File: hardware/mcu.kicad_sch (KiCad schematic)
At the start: 0 parts

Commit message: ✨ Further power supply schematic
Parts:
- added U1: ~, PCM_Espressif:ESP32-P4, symbol PCM_Espressif:ESP32-P4

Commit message: ✨ Further schematic updates
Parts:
- added C29: 100nF/10V, symbol Device:C
- added R13: 10k, symbol Device:R
- added U7: W25Q128JVP, Package_SON:WSON-8-1EP_6x5mm_P1.27mm_EP3.4x4.3mm, symbol Memory_Flash:W25Q128JVP
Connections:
- net +3.3VA: now reaches U1.101 (VDD_ANA)
- net +3.3V: now reaches U1.102 (VDD_BAT)
- net +3.3V: now also U1.21 (VDD_IO_0), U1.30 (VDD_FLASH_IO), U1.51 (VDD_USBPHY), U1.62 (VDD_IO_4), U1.75 (VDD_LDO), U1.85 (VDD_IO_5), U1.9 (VDD_LP), U1.96 (VDD_IO_6), C29.1, R13.1, U7.8 (VCC)
- net GND: now reaches U1.105 (GND)
- net GND: now also C29.2, U7.4 (GND), U7.9 (EP)
- net +1V2: now reaches U1.26 (VDD_HP_0)
- net +1V2: now also U1.76 (VDD_HP_2), U1.91 (VDD_HP_3)
- net FLASH_CS: now reaches U1.27 (FLASH_CS)
- net FLASH_CS: now also R13.2, U7.1 (~{CS})
- net FLASH_Q: now reaches U1.28 (FLASH_Q)
- net FLASH_Q: now also U7.2 (DO/IO_{1})
- net FLASH_WP: now reaches U1.29 (FLASH_WP)
- net FLASH_WP: now also U7.3 (~{WP}/IO_{2})
- net FLASH_HOLD: now reaches U1.31 (FLASH_HOLD)
- net FLASH_HOLD: now also U7.7 (~{HOLD}/~{RESET}/IO_{3})
- net FLASH_CK: now reaches U1.32 (FLASH_CK)
- net FLASH_CK: now also U7.6 (CLK)
- net FLASH_D: now reaches U1.33 (FLASH_D)
- net FLASH_D: now also U7.5 (DI/IO_{0})
- net +2V5: now reaches U1.41 (VDD_MIPI_DPHY)
- net FB_DCDC: now reaches U1.78 (FB_DCDC)
- net EN_DCDC: now reaches U1.79 (EN_DCDC)

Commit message: ✨ MCU updates
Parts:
- added C39, C40: 12pF, symbol Device:C
- added C41, C42, C43, C44: 1uF, symbol Device:C
- added C45, C46, C47, C48, C49, C50, C51, C52, C53, C54, C55, C56, C57, C58, C59, C60: 100nF, symbol Device:C
- added R21, R22: 0, symbol Device:R
- added R23: 4.02k, symbol Device:R
- added X1: ECS-400-10-37B2-CKY-TR, Crystal:Crystal_SMD_2016-4Pin_2.0x1.6mm, symbol PCM_Crystal_AKL:Crystal_Generic_GND24
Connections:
- net +1V2: now also C46.1, C49.1, C50.1
- net +2V5: now also C52.1
- net +3.3V: now also U1.77 (VDD_DCDCC), C45.1, C51.1, C53.1, C54.1, C55.1, C56.1, C57.1, C59.1, C60.1
- net +3.3VA: now also C58.1
- net GND: now also C39.2, C40.2, C41.2, C42.2, C43.2, C44.2, C45.2, C46.2, C47.2, C48.2, C49.2, C50.2, C51.2, C52.2, C53.2, C54.2, C55.2, C56.2, C57.2, C58.2, C59.2, C60.2, R23.2, X1.2, X1.4
- net XTAL_P: now reaches U1.100 (XTAL_P)
- net XTAL_P: now also R21.1
- net at U1.34 (DSI_REXT): now also R23.1
- net VDDO_PSRAM: now reaches U1.59 (VDD_PSRAM_0)
- net VDDO_PSRAM: now also U1.67 (VDD_PSRAM_1), U1.72 (VDDO_PSRAM), C42.1, C47.1, C48.1
- net VDDO_FLASH: now reaches U1.71 (VDDO_FLASH)
- net VDDO_FLASH: now also C41.1
- net VDDO_3: now reaches U1.73 (VDDO_3)
- net VDDO_3: now also C43.1
- net VDDO_4: now reaches U1.74 (VDDO_4)
- net VDDO_4: now also C44.1
- net XTAL_N: now reaches U1.99 (XTAL_N)
- net XTAL_N: now also R22.2
- new net: C39.1, R21.2, X1.1
- new net: C40.1, R22.1, X1.3

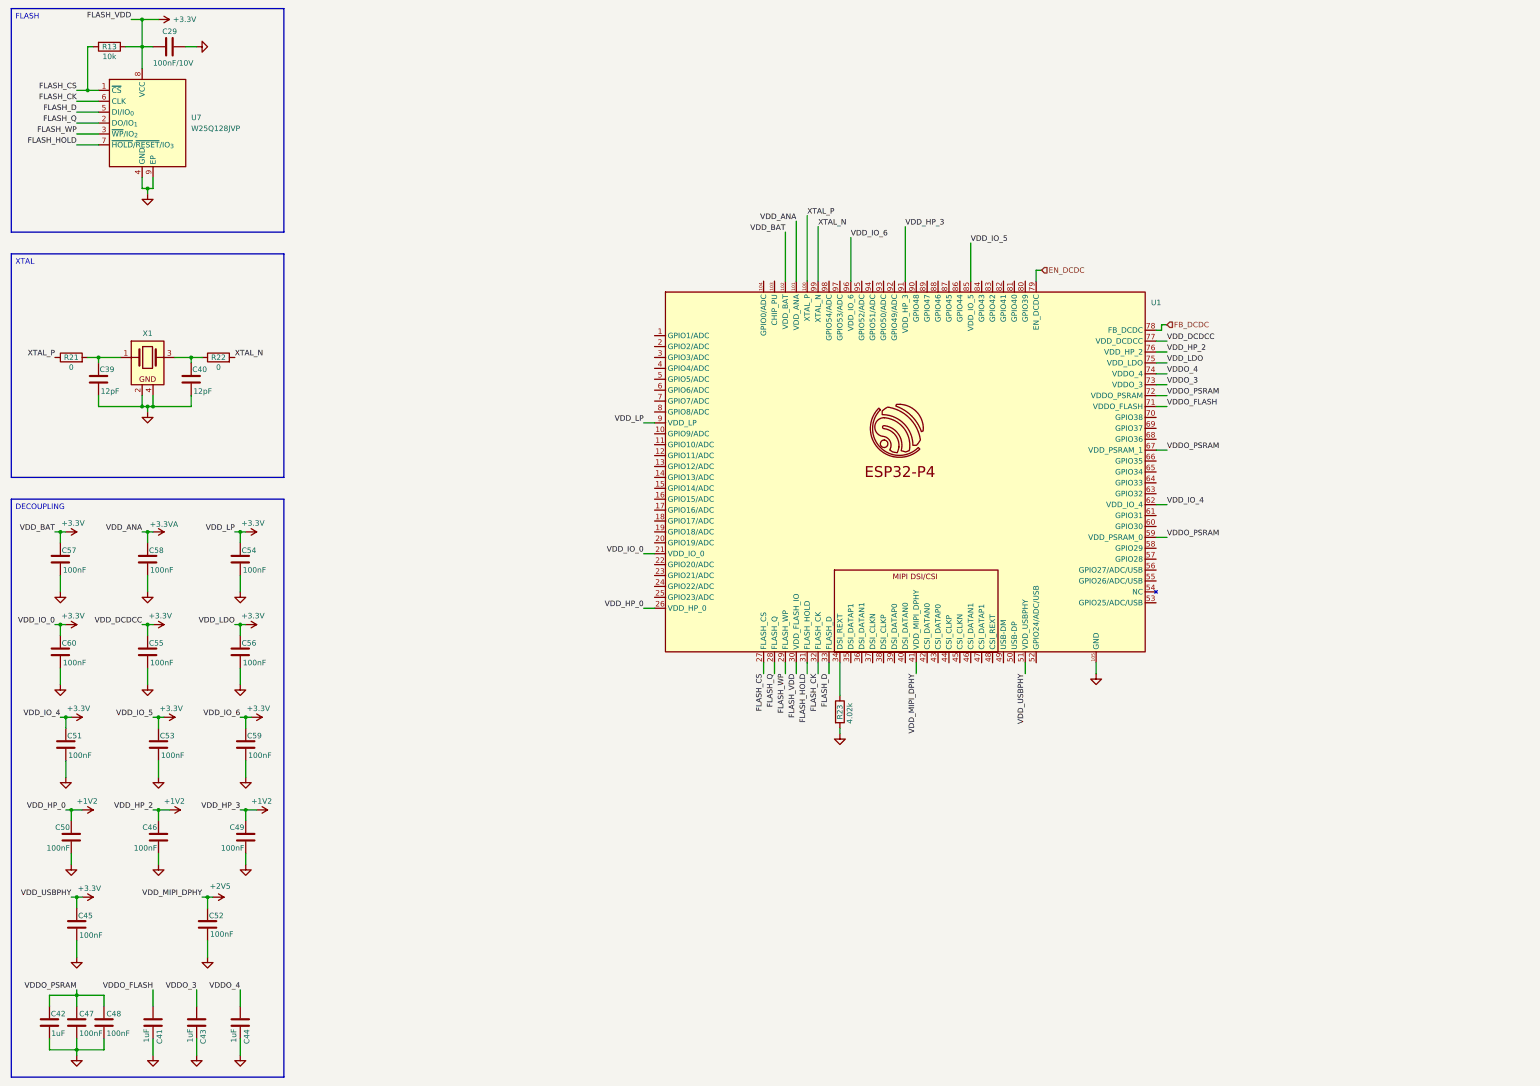
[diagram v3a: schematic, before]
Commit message: ✨ Done wireless schematic
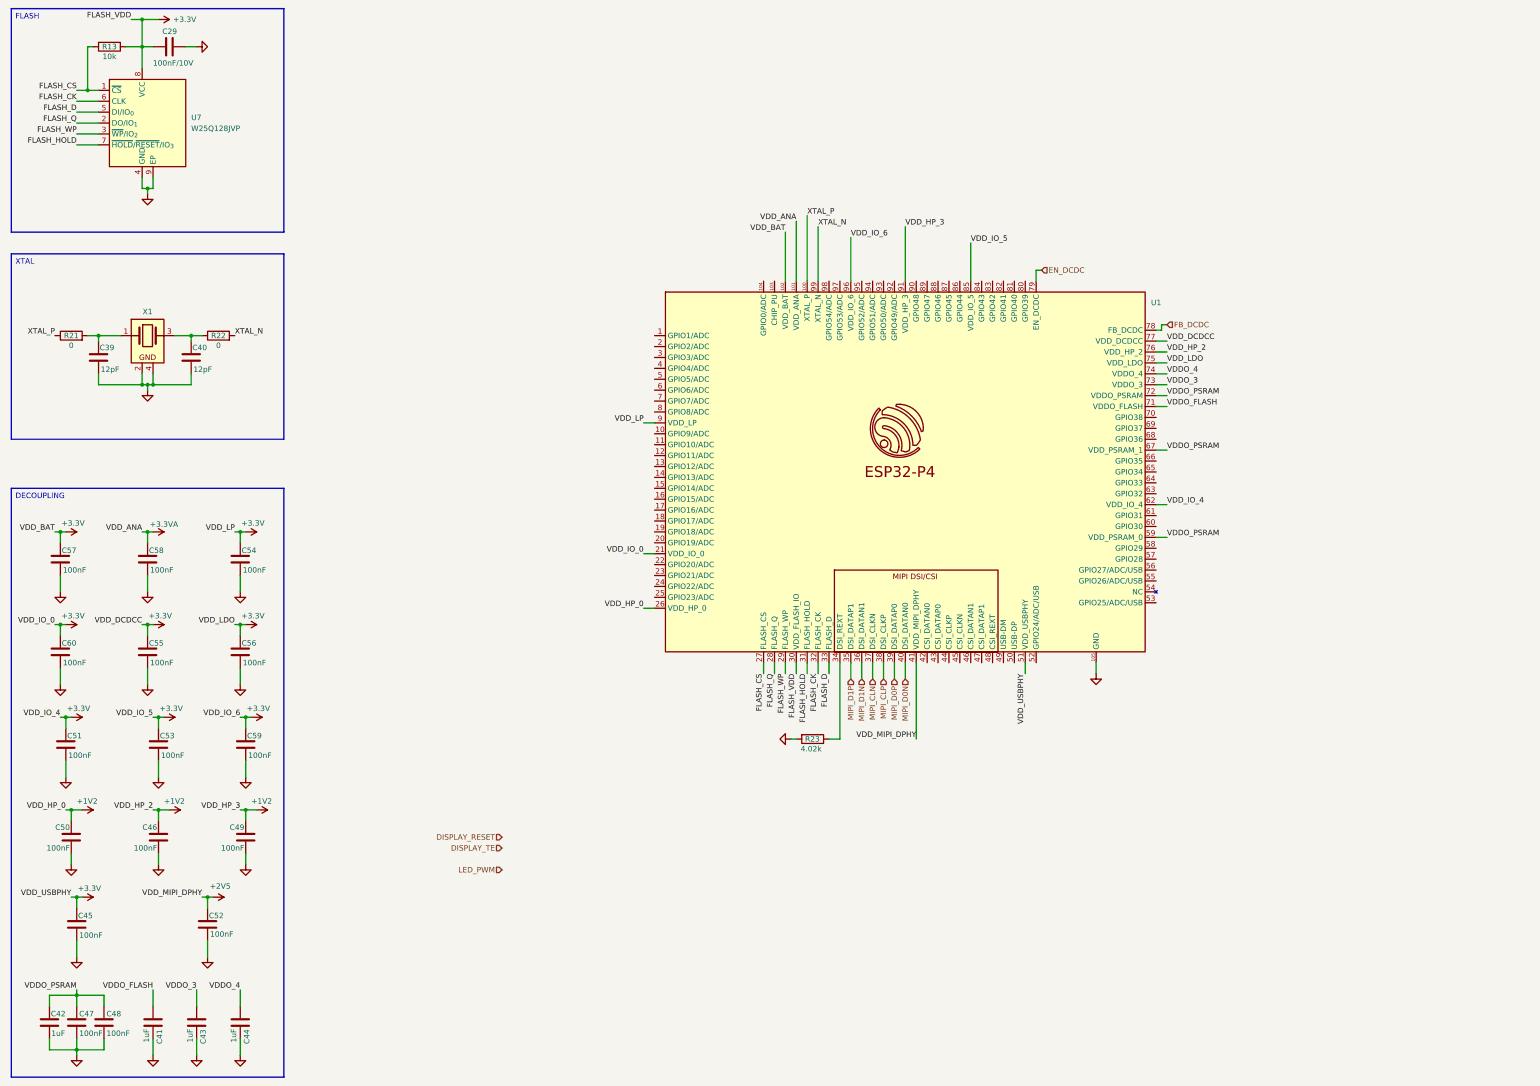
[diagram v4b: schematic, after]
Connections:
- net MIPI_D1P: now reaches U1.35 (DSI_DATAP1)
- net MIPI_D1N: now reaches U1.36 (DSI_DATAN1)
- net MIPI_CLN: now reaches U1.37 (DSI_CLKN)
- net MIPI_CLP: now reaches U1.38 (DSI_CLKP)
- net MIPI_D0P: now reaches U1.39 (DSI_DATAP0)
- net MIPI_D0N: now reaches U1.40 (DSI_DATAN0)
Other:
- moved on the sheet: C39, C40, R21, R22, R23, X1

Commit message: 📂 PCB updates
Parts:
- added C18: 1uF, Capacitor_SMD:C_0402_1005Metric, symbol Device:C
- added J4: Conn_DEBUG_P4, Connector_JST:JST_SHL_SM06B-SHLS-TF_1x06-1MP_P1.00mm_Horizontal, symbol Connector_Generic:Conn_01x06
- added R36, R37, R38, R39, R40, R41: 0, PCM_Resistor_SMD_AKL:R_0402_1005Metric, symbol Device:R
- added R42, R43: 4.7k, PCM_Resistor_SMD_AKL:R_0402_1005Metric, symbol Device:R
- added R44, R45: 10k, PCM_Resistor_SMD_AKL:R_0402_1005Metric, symbol Device:R
- C29: value 100nF/10V -> 100nF; footprint (none) -> Capacitor_SMD:C_0402_1005Metric
- C39, C40, C41, C42, C43, C44, C45, C46, C47, C48, C49, C50, C51, C52, C53, C54, C55, C56, C57, C58, C59, C60: footprint (none) -> Capacitor_SMD:C_0402_1005Metric
- R13, R21, R22, R23: footprint (none) -> PCM_Resistor_SMD_AKL:R_0402_1005Metric
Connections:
- net +3.3V: now also R42.2, R43.2, R44.1, R45.1
- net DISPLAY_RESET: now also U1.57 (GPIO28)
- net DISPLAY_TE: now also U1.56 (GPIO27/ADC/USB)
- net GND: now also C18.2, J4.6 (Pin_6)
- net LED_PWM: now also U1.55 (GPIO26/ADC/USB)
- net MIPI_CLN: now also R38.1; no longer U1.37 (DSI_CLKN)
- net MIPI_CLP: now also R39.1; no longer U1.38 (DSI_CLKP)
- net MIPI_D0N: now also R41.1; no longer U1.40 (DSI_DATAN0)
- net MIPI_D0P: now also R40.1; no longer U1.39 (DSI_DATAP0)
- net MIPI_D1N: now also R37.1; no longer U1.36 (DSI_DATAN1)
- net MIPI_D1P: now also R36.1; no longer U1.35 (DSI_DATAP1)
- net SW_MCU: now reaches U1.10 (GPIO9/ADC)
- net EN: now reaches U1.103 (CHIP_PU)
- net EN: now also C18.1, J4.2 (Pin_2), R44.2
- net SDIO_DATA0: now reaches U1.15 (GPIO14/ADC)
- net SDIO_DATA1: now reaches U1.16 (GPIO15/ADC)
- net SDIO_DATA2: now reaches U1.17 (GPIO16/ADC)
- net SDIO_DATA3: now reaches U1.18 (GPIO17/ADC)
- net SDIO_CLK: now reaches U1.19 (GPIO18/ADC)
- net SDIO_CMD: now reaches U1.20 (GPIO19/ADC)
- net RX_CAN: now reaches U1.23 (GPIO21/ADC)
- net TX_CAN: now reaches U1.24 (GPIO22/ADC)
- net JTAG_DN: now reaches U1.49 (USB-DM)
- net JTAG_DN: now also J4.5 (Pin_5)
- net JTAG_DP: now reaches U1.50 (USB-DP)
- net JTAG_DP: now also J4.4 (Pin_4)
- net BUTTON_U: now reaches U1.6 (GPIO6/ADC)
- net SCL_MCU: now reaches U1.60 (GPIO30)
- net SCL_MCU: now also R43.1
- net SDA_MCU: now reaches U1.61 (GPIO31)
- net SDA_MCU: now also R42.1
- net BOOT: now reaches U1.66 (GPIO35)
- net BOOT: now also J4.3 (Pin_3)
- net at U1.68 (GPIO36): now also R45.2
- net BUTTON_P: now reaches U1.7 (GPIO7/ADC)
- net BUTTON_D: now reaches U1.8 (GPIO8/ADC)
- net VBUS_MCU: now reaches U1.92 (GPIO49/ADC)
- new net +5V: J4.1 (Pin_1)
- new net MIPI_MCU_CLN: R38.2, U1.37 (DSI_CLKN)
- new net MIPI_MCU_CLP: R39.2, U1.38 (DSI_CLKP)
- new net MIPI_MCU_D0N: R41.2, U1.40 (DSI_DATAN0)
- new net MIPI_MCU_D0P: R40.2, U1.39 (DSI_DATAP0)
- new net MIPI_MCU_D1N: R37.2, U1.36 (DSI_DATAN1)
- new net MIPI_MCU_D1P: R36.2, U1.35 (DSI_DATAP1)

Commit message: 🐛 Fix errors from rev1.0
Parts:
- removed C52: 100nF, Capacitor_SMD:C_0402_1005Metric, symbol Device:C
- added C10: 100nF, Capacitor_SMD:C_0402_1005Metric, symbol Device:C
- added R46, R47: 33, PCM_Resistor_SMD_AKL:R_0603_1608Metric, symbol Device:R
- added R48: 4.02k, PCM_Resistor_SMD_AKL:R_0402_1005Metric, symbol Device:R
- added R51: 10k, PCM_Resistor_SMD_AKL:R_0402_1005Metric, symbol Device:R
- C18: value 1uF -> 100nF
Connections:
- net +2V5 is gone; now on net VDDO_3: U1.41 (VDD_MIPI_DPHY)
- net +3.3V: now also R51.1
- net BOOT: now also R51.2
- net DISPLAY_RESET: now also U1.13 (GPIO12/ADC); no longer U1.57 (GPIO28)
- net DISPLAY_TE: now also U1.12 (GPIO11/ADC); no longer U1.56 (GPIO27/ADC/USB)
- net GND: now also C10.2, R48.2
- net JTAG_DN: now also U1.52 (GPIO24/ADC/USB), R46.2; no longer J4.5 (Pin_5), U1.49 (USB-DM)
- net JTAG_DP: now also U1.53 (GPIO25/ADC/USB), R47.2; no longer J4.4 (Pin_4), U1.50 (USB-DP)
- net LED_PWM: now also U1.11 (GPIO10/ADC); no longer U1.55 (GPIO26/ADC/USB)
- net VDDO_3: now also C10.1
- net at U1.48 (CSI_REXT): now also R48.1
- net C6_WKUP: now reaches U1.5 (GPIO5/ADC)
- new net: J4.4 (Pin_4), R47.1
- new net: J4.5 (Pin_5), R46.1

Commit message: ✨ Finish rev 1.1
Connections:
- net XTAL_N: now also C40.1
- net XTAL_P: now also C39.1
- net at R21.2, X1.1: no longer C39.1
- net at R22.1, X1.3: no longer C40.1
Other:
- moved on the sheet: C39, C40, R21, R22
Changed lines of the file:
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@@
 	)
 	(junction
-		(at 55.88 144.78)
+		(at 39.37 99.06)
 		(diameter 0)
 		(color 0 0 0 0)
 	)
 	(junction
-		(at 58.42 187.96)
+		(at 55.88 144.78)
 		(diameter 0)
 		(color 0 0 0 0)
 	)
 	(junction
-		(at 41.91 41.91)
+		(at 58.42 187.96)
 		(diameter 0)
 		(color 0 0 0 0)
 	)
 	(junction
-		(at 35.56 166.37)
+		(at 41.91 41.91)
 		(diameter 0)
 		(color 0 0 0 0)
 	)
 	(junction
-		(at 44.45 99.06)
+		(at 35.56 166.37)
 		(diameter 0)
 		(color 0 0 0 0)
@@
 	)
 	(junction
-		(at 66.04 99.06)
+		(at 72.39 99.06)
 		(diameter 0)
 		(color 0 0 0 0)
@@
 	(wire
 		(pts
+			(xy 72.39 99.06) (xy 76.2 99.06)
+		)
+		(stroke
+			(width 0)
+			(type default)
+		)
+	)
+	(wire
+		(pts
 			(xy 54.61 31.75) (xy 57.15 31.75)
 		)
@@
 	(wire
 		(pts
-			(xy 222.25 175.26) (xy 222.25 190.5)
+			(xy 39.37 99.06) (xy 34.29 99.06)
 		)
 		(stroke
@@
 	(wire
 		(pts
-			(xy 39.37 240.03) (xy 39.37 243.84)
+			(xy 222.25 175.26) (xy 222.25 190.5)
 		)
 		(stroke
@@
 	(wire
 		(pts
-			(xy 370.84 186.69) (xy 370.84 191.77)
+			(xy 39.37 240.03) (xy 39.37 243.84)
 		)
 		(stroke
@@
 	(wire
 		(pts
-			(xy 57.15 187.96) (xy 58.42 187.96)
+			(xy 370.84 186.69) (xy 370.84 191.77)
 		)
 		(stroke
@@
 	(wire
 		(pts
-			(xy 293.37 127) (xy 293.37 125.73)
+			(xy 57.15 187.96) (xy 58.42 187.96)
 		)
 		(stroke
@@
 	(wire
 		(pts
-			(xy 44.45 99.06) (xy 49.53 99.06)
+			(xy 293.37 127) (xy 293.37 125.73)
 		)
 		(stroke
@@
 	(wire
 		(pts
-			(xy 44.45 99.06) (xy 44.45 100.33)
+			(xy 39.37 99.06) (xy 39.37 100.33)
 		)
 		(stroke
@@
 	(wire
 		(pts
+			(xy 71.12 99.06) (xy 72.39 99.06)
+		)
+		(stroke
+			(width 0)
+			(type default)
+		)
+	)
+	(wire
+		(pts
 			(xy 171.45 114.3) (xy 173.99 114.3)
 		)
@@
 	(wire
 		(pts
+			(xy 48.26 99.06) (xy 49.53 99.06)
+		)
+		(stroke
+			(width 0)
+			(type default)
+		)
+	)
+	(wire
+		(pts
 			(xy 78.74 209.55) (xy 81.28 209.55)
 		)
@@
 	(wire
 		(pts
-			(xy 62.23 99.06) (xy 66.04 99.06)
+			(xy 62.23 99.06) (xy 63.5 99.06)
 		)
 		(stroke
@@
 	(wire
 		(pts
-			(xy 44.45 107.95) (xy 44.45 110.49)
+			(xy 39.37 107.95) (xy 39.37 110.49)
 		)
 		(stroke
@@
 	(wire
 		(pts
-			(xy 66.04 107.95) (xy 66.04 110.49)
-		)
-		(stroke
-			(width 0)
-			(type default)
-		)
-	)
-	(wire
-		(pts
-			(xy 66.04 99.06) (xy 68.58 99.06)
+			(xy 72.39 107.95) (xy 72.39 110.49)
 		)
 		(stroke
@@
 	(wire
 		(pts
-			(xy 66.04 99.06) (xy 66.04 100.33)
+			(xy 72.39 99.06) (xy 72.39 100.33)
 		)
 		(stroke
@@
 	(wire
 		(pts
-			(xy 41.91 99.06) (xy 44.45 99.06)
-		)
-		(stroke
-			(width 0)
-			(type default)
-		)
-	)
-	(wire
-		(pts
 			(xy 57.15 110.49) (xy 55.88 110.49)
 		)
@@
 	(wire
 		(pts
-			(xy 44.45 110.49) (xy 54.61 110.49)
+			(xy 39.37 110.49) (xy 54.61 110.49)
 		)
 		(stroke
@@
 	(wire
 		(pts
-			(xy 66.04 110.49) (xy 57.15 110.49)
+			(xy 72.39 110.49) (xy 57.15 110.49)
 		)
 		(stroke
@@
 	(wire
 		(pts
+			(xy 40.64 99.06) (xy 39.37 99.06)
+		)
+		(stroke
+			(width 0)
+			(type default)
+		)
+	)
+	(wire
+		(pts
 			(xy 39.37 252.73) (xy 33.02 252.73)
 		)
@@
 	(symbol
 		(lib_id "Device:C")
-		(at 44.45 104.14 0)
+		(at 39.37 104.14 0)
 		(unit 1)
 		(exclude_from_sim no)
@@
 		(dnp no)
 		(property "Reference" "C39"
-			(at 44.704 101.854 0)
+			(at 39.624 101.854 0)
 			(effects
 				(font
@@
 		)
 		(property "Value" "12pF"
-			(at 44.958 106.934 0)
+			(at 39.878 106.934 0)
 			(effects
 				(font
@@
 		)
 		(property "Footprint" "Capacitor_SMD:C_0402_1005Metric"
-			(at 45.4152 107.95 0)
+			(at 40.3352 107.95 0)
 			(effects
 				(font
@@
 		)
 		(property "Datasheet" "~"
-			(at 44.45 104.14 0)
+			(at 39.37 104.14 0)
 			(effects
 				(font
@@
 		)
 		(property "Description" "Unpolarized capacitor"
-			(at 44.45 104.14 0)
+			(at 39.37 104.14 0)
 			(effects
 				(font
@@
 	(symbol
 		(lib_id "Device:R")
-		(at 72.39 99.06 90)
+		(at 67.31 99.06 90)
 		(unit 1)
 		(exclude_from_sim no)
@@
 		(dnp no)
 		(property "Reference" "R22"
-			(at 72.39 99.06 90)
+			(at 67.31 99.06 90)
 			(effects
 				(font
@@
 		)
 		(property "Value" "0"
-			(at 72.39 101.346 90)
+			(at 67.31 101.346 90)
 			(effects
 				(font
@@
 		)
 		(property "Footprint" "PCM_Resistor_SMD_AKL:R_0402_1005Metric"
-			(at 72.39 100.838 90)
+			(at 67.31 100.838 90)
 			(effects
 				(font
@@
 		)
 		(property "Datasheet" "~"
-			(at 72.39 99.06 0)
+			(at 67.31 99.06 0)
 			(effects
 				(font
@@
 		)
 		(property "Description" "Resistor"
-			(at 72.39 99.06 0)
+			(at 67.31 99.06 0)
 			(effects
 				(font
@@
 	(symbol
 		(lib_id "Device:C")
-		(at 66.04 104.14 0)
+		(at 72.39 104.14 0)
 		(unit 1)
 		(exclude_from_sim no)
@@
 		(dnp no)
 		(property "Reference" "C40"
-			(at 66.294 101.854 0)
+			(at 72.644 101.854 0)
 			(effects
 				(font
@@
 		)
 		(property "Value" "12pF"
-			(at 66.548 106.934 0)
+			(at 72.898 106.934 0)
 			(effects
 				(font
@@
 		)
 		(property "Footprint" "Capacitor_SMD:C_0402_1005Metric"
-			(at 67.0052 107.95 0)
+			(at 73.3552 107.95 0)
 			(effects
 				(font
@@
 		)
 		(property "Datasheet" "~"
-			(at 66.04 104.14 0)
+			(at 72.39 104.14 0)
 			(effects
 				(font
@@
 		)
 		(property "Description" "Unpolarized capacitor"
-			(at 66.04 104.14 0)
+			(at 72.39 104.14 0)
 			(effects
 				(font
@@
 	(symbol
 		(lib_id "Device:R")
-		(at 38.1 99.06 90)
+		(at 44.45 99.06 90)
 		(unit 1)
 		(exclude_from_sim no)
@@
 		(dnp no)
 		(property "Reference" "R21"
-			(at 38.1 99.06 90)
+			(at 44.45 99.06 90)
 			(effects
 				(font
@@
 		)
 		(property "Value" "0"
-			(at 38.1 101.346 90)
+			(at 44.45 101.346 90)
 			(effects
 				(font
@@
 		)
 		(property "Footprint" "PCM_Resistor_SMD_AKL:R_0402_1005Metric"
-			(at 38.1 100.838 90)
+			(at 44.45 100.838 90)
 			(effects
 				(font
@@
 		)
 		(property "Datasheet" "~"
-			(at 38.1 99.06 0)
+			(at 44.45 99.06 0)
 			(effects
 				(font
@@
 		)
 		(property "Description" "Resistor"
-			(at 38.1 99.06 0)
+			(at 44.45 99.06 0)
 			(effects
 				(font

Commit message: ✨ Final PCB updates
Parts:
- R17: renamed from R47; footprint PCM_Resistor_SMD_AKL:R_0603_1608Metric -> PCM_Resistor_SMD_AKL:R_0402_1005Metric
- R18: renamed from R46; footprint PCM_Resistor_SMD_AKL:R_0603_1608Metric -> PCM_Resistor_SMD_AKL:R_0402_1005Metric
- renumbered C39 to C1, C51 to C10, C53 to C11, C59 to C12, C50 to C13, C46 to C14, C49 to C15, C45 to C16, C42 to C17, C47 to C18, C48 to C19, C40 to C2, C41 to C20, C43 to C21, C44 to C22, C10 to C23, C18 to C24, C29 to C3, C57 to C4, C58 to C5, C54 to C6, C60 to C7, C55 to C8, C56 to C9, R21 to R1, R41 to R10, R48 to R11, R45 to R12, R51 to R13, R44 to R14, R42 to R15, R43 to R16, R22 to R2, R13 to R3, R23 to R4, R36 to R5, R37 to R6, R38 to R7, R39 to R8, R40 to R9, U7 to U2
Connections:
- net +3.3V: no longer C11.1, U1.85 (VDD_IO_5)
- net DISPLAY_RESET: now also U1.81 (GPIO40); no longer U1.13 (GPIO12/ADC)
- net DISPLAY_TE: now also U1.80 (GPIO39); no longer U1.12 (GPIO11/ADC)
- net XTAL_N: no longer C2.1
- net XTAL_P: no longer C1.1
- net at R1.2, X1.1: now also C1.1
- net at R2.1, X1.3: now also C2.1
- new net +1V8: C11.1, U1.85 (VDD_IO_5)
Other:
- moved on the sheet: C1, C2, R1, R2
